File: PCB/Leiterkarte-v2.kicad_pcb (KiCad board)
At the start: 4 copper layers, 40.3 x 85.7 mm, 56 parts

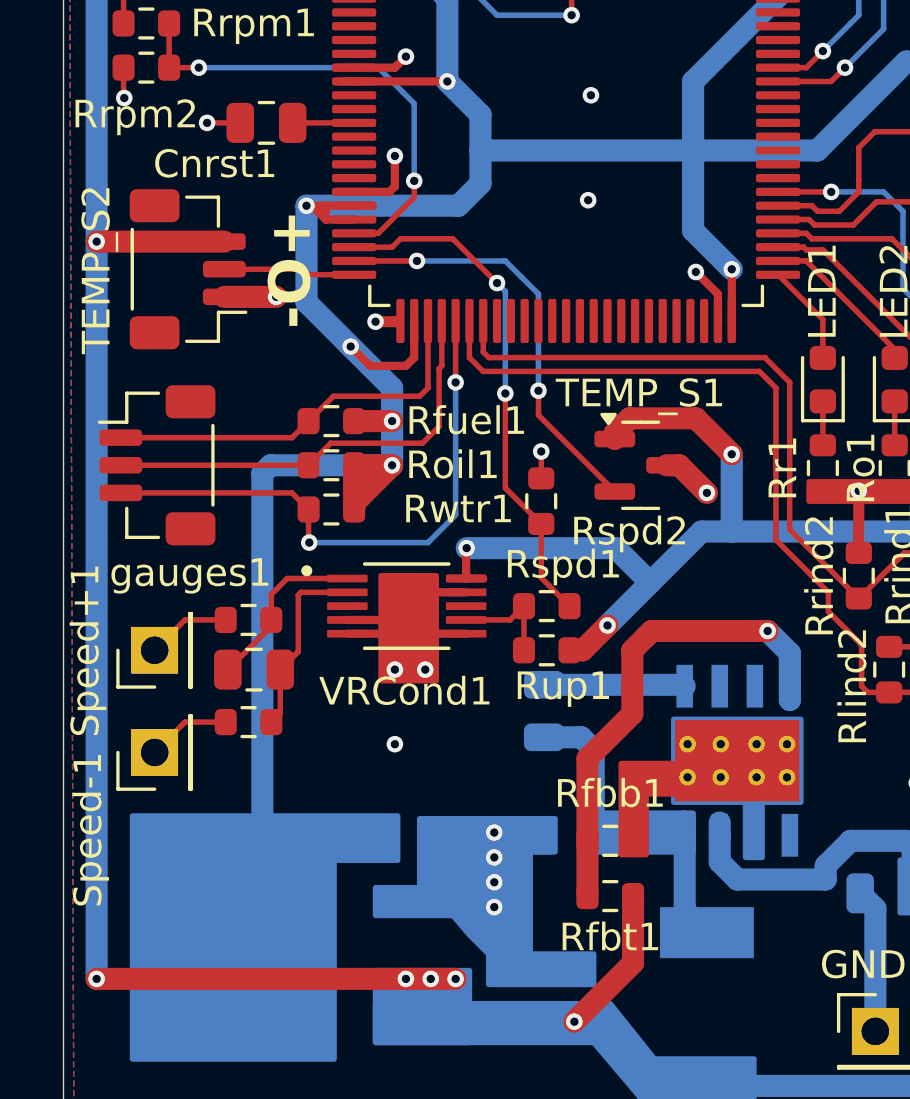
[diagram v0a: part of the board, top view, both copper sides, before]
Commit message: Replaced Speed- and Speed+ solder faces with JST SH connector
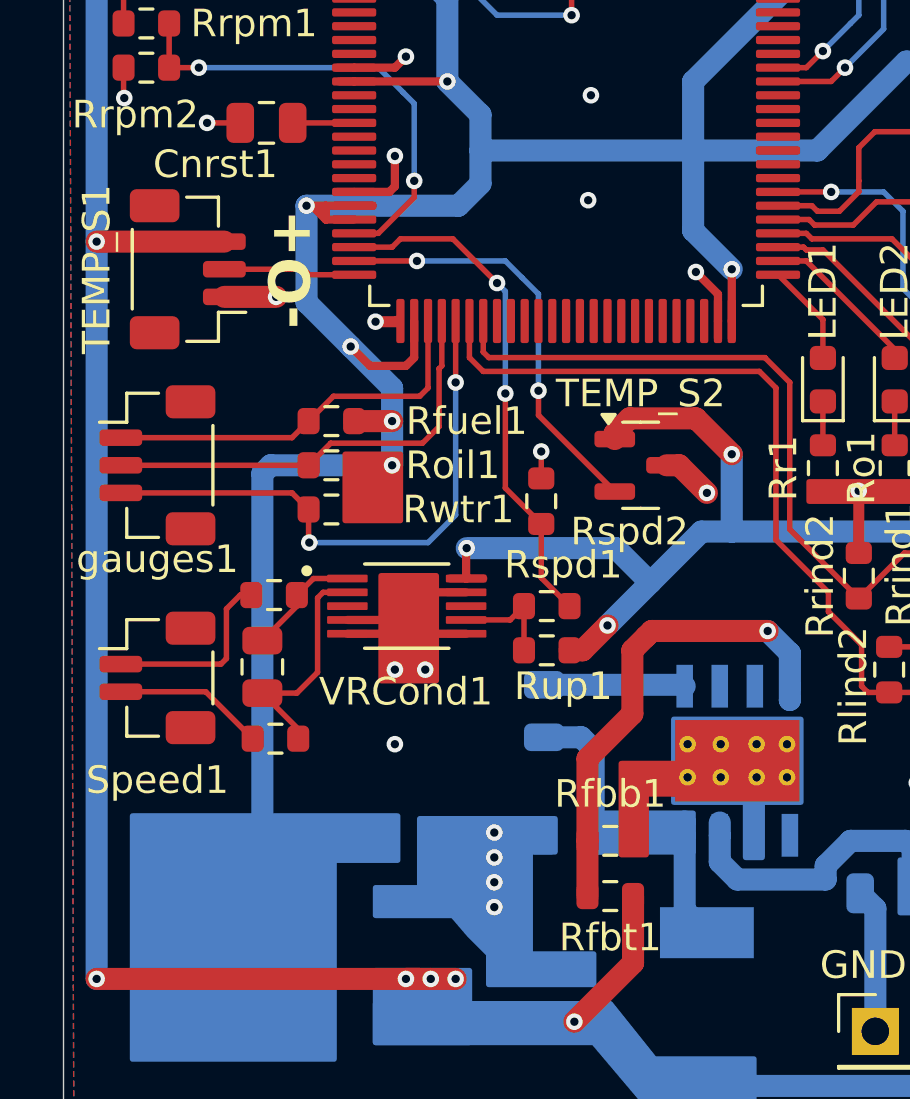
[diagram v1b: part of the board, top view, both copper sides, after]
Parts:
- removed Speed+1, Speed-1: Conn_01x01_Pin, Connector_PinHeader_2.54mm:PinHeader_1x01_P2.54mm_Vertical
- added Speed1: Conn_01x02_Pin, Connector_JST:JST_SH_BM02B-SRSS-TB_1x02-1MP_P1.00mm_Vertical, F.Cu at (147.8, 110.4)
- moved R2 1.29 mm to (152.0, 107.4)
- moved R1 1.14 mm to (152.1, 112.6)
- moved Cmax1 0.32 mm to (151.6, 110.0), turned to 90 degrees
- renumbered TEMP_S2 to TEMP_S1, TEMP_S1 to TEMP_S2
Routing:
- net +3.3V: track 155.6 -> 150.7 mm
- net Net-(Speed1-Pin_1): track 3.03 -> 6.81 mm
- net Net-(Speed1-Pin_2): track 3.03 -> 5.48 mm
- net Net-(VRCond1-IN+): track 6.37 -> 4.25 mm
- net Net-(VRCond1-IN-): track 6.83 -> 8.36 mm

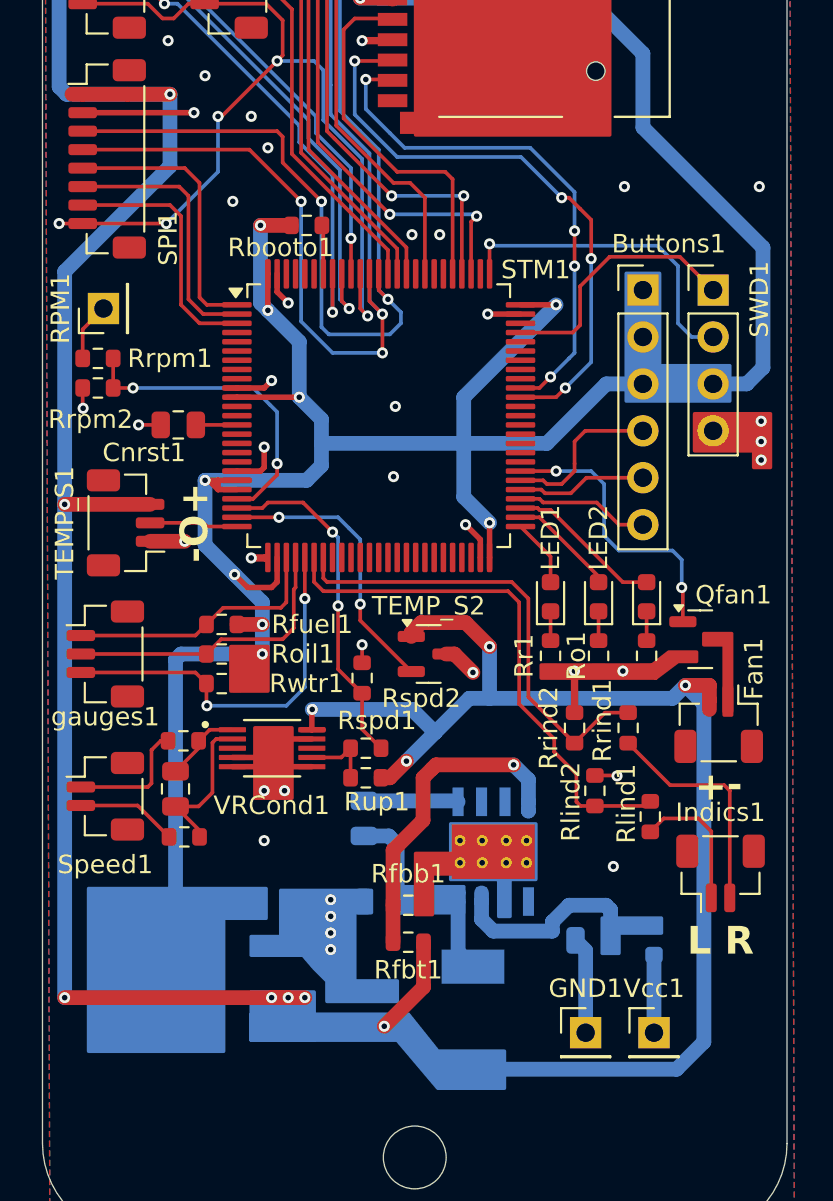
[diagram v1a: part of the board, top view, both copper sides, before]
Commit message: Replaced capacitor Cout2 and moved it to other side of the PCB;Updated some resistor footprints (to 0805);Some other stuff I forgot but similar :)
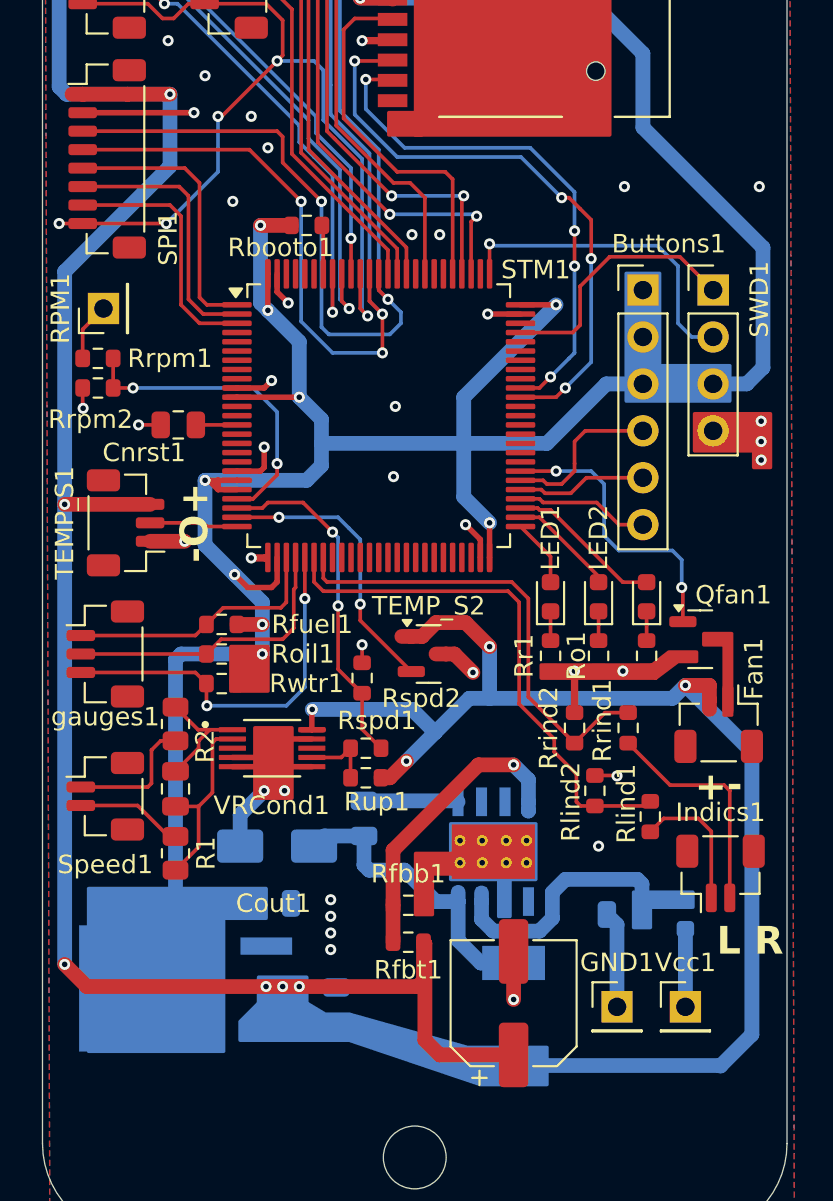
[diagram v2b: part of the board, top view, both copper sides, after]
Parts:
- Cout2: value 330uF -> 220uF; footprint Capacitor_SMD:C_0805_2012Metric -> Capacitor_SMD:CP_Elec_6.3x5.9; moved to F.Cu
- D1: footprint Diode_SMD:D_0805_2012Metric -> Diode_SMD:D_SMA
- R1, R2: footprint Resistor_SMD:R_0603_1608Metric -> Resistor_SMD:R_0805_2012Metric
- moved Cout2 7.01 mm to (169.9, 121.6)
- moved D1 6.35 mm to (157.1, 113.1)
- moved L1 2.21 mm to (169.9, 122.2)
- moved Cin1 2.20 mm to (175.9, 116.8)
- moved F1 2.20 mm to (179.2, 116.8)
- moved GND1 2.20 mm to (175.5, 121.8)
- moved Vcc1 2.20 mm to (179.2, 121.8)
- moved R2 1.01 mm to (151.6, 106.5), turned to 90 degrees
- moved R1 1.01 mm to (151.6, 113.5), turned to -90 degrees
- moved 3.3V1 0.55 mm to (150.1, 120.8)
- moved Cin2 0.28 mm to (160.3, 121.7)
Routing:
- net +5V: track 180.2 -> 193.6 mm, vias 12 -> 11
- net GND: track 67.4 -> 75.1 mm
- net Net-(5V1-PH): track 9.46 -> 16.5 mm
- net VCC: track 11.3 -> 14.1 mm
- net Net-(VRCond1-IN+): track 4.25 -> 6.60 mm
- net Net-(VRCond1-IN-): track 8.36 -> 10.1 mm
- net Net-(5V1-VSENSE): track 17.6 -> 16.3 mm

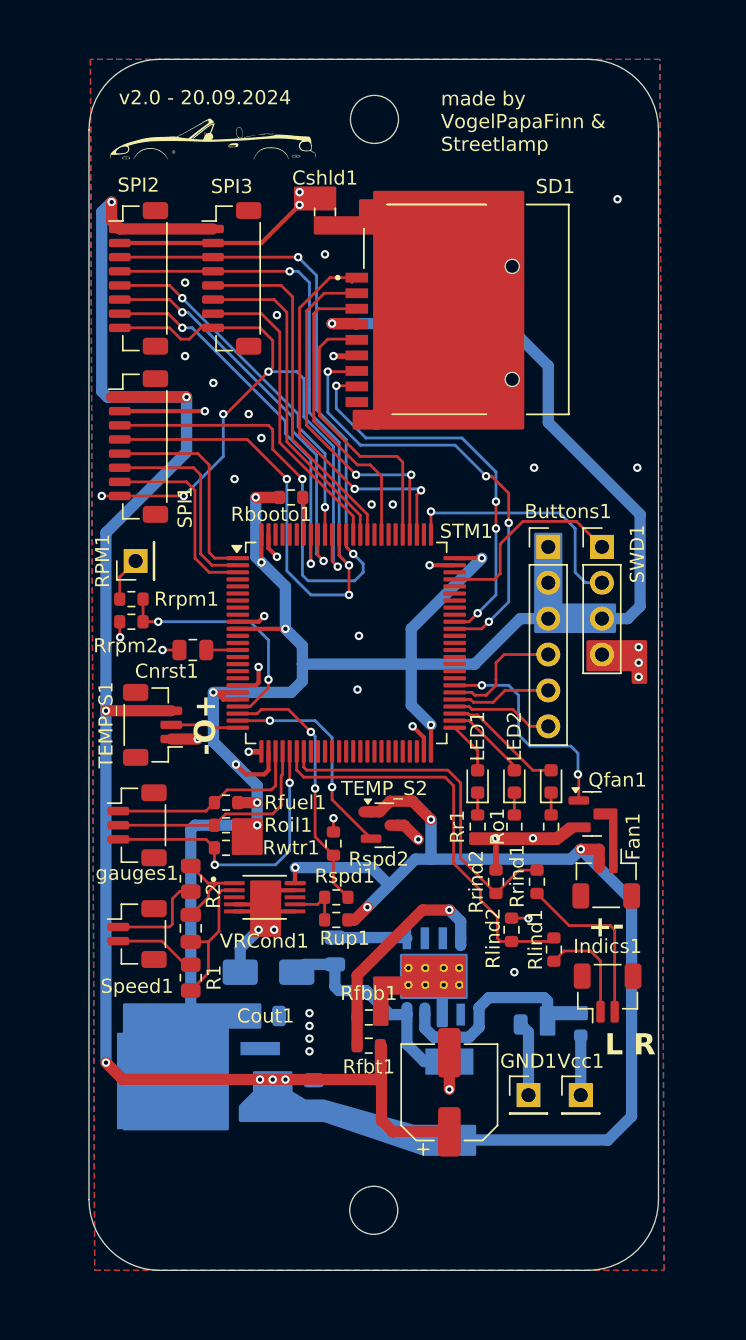
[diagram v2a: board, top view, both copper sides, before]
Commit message: Replaced STM32 with ESP32; Addec circuitry for ESP32; Removed LEDs; Added USB-C for flashing
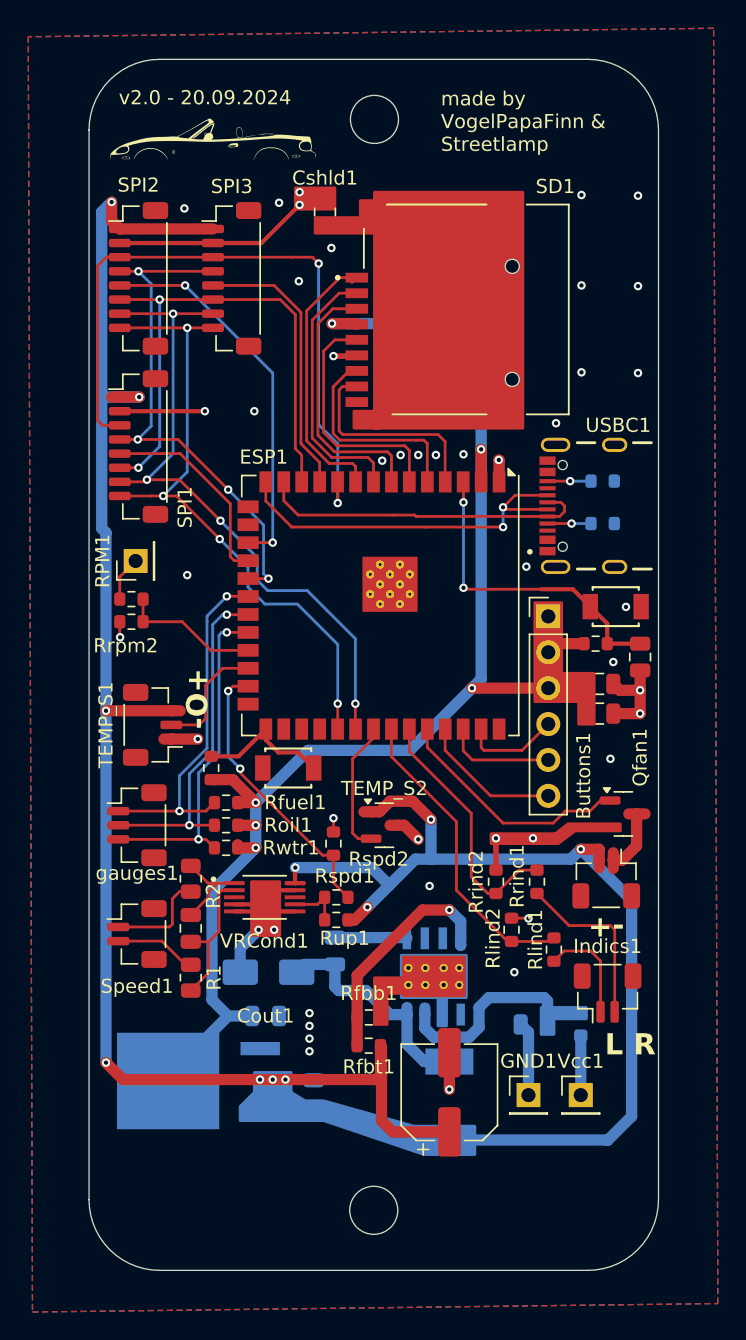
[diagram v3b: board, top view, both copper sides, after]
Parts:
- removed Cnrst1: 100nF, Capacitor_SMD:C_0805_2012Metric
- removed LED1: Red, LED_SMD:LED_0603_1608Metric
- removed LED2: Orange, LED_SMD:LED_0603_1608Metric
- removed LED3: Green, LED_SMD:LED_0603_1608Metric
- removed Rbooto1: 10K, Resistor_SMD:R_0603_1608Metric
- removed Rg1: 30, Resistor_SMD:R_0603_1608Metric
- removed Ro1, Rr1: 150, Resistor_SMD:R_0603_1608Metric
- removed STM1: STM32H743VITx, Package_QFP:LQFP-100_14x14mm_P0.5mm
- removed SWD1: Conn_01x04_Pin, Connector_PinHeader_2.54mm:PinHeader_1x04_P2.54mm_Vertical
- added Cen1: 1uF, Capacitor_SMD:C_0805_2012Metric, F.Cu at (183.4, 90.8)
- added Cesp1: 22uF, Capacitor_SMD:C_0805_2012Metric, F.Cu at (180.6, 94.8)
- added Cesp2: 0.1uF, Capacitor_SMD:C_0805_2012Metric, F.Cu at (180.6, 92.7)
- added ESP1: ESP32-S3-WROOM-1U, RF_Module:ESP32-S3-WROOM-1U, F.Cu at (165.0, 87.2)
- added ESP_BOOT1: SW_SPST, button:small_button, F.Cu at (158.5, 98.7)
- added ESP_RST1: SW_SPST, button:small_button, F.Cu at (181.7, 87.2)
- added Rboot1: 10k, Resistor_SMD:R_0603_1608Metric, F.Cu at (153.1, 98.7)
- added Resp1: 5.1k, Resistor_SMD:R_0603_1608Metric, F.Cu at (180.2, 89.8)
- added Rusb1: 5.1k, Resistor_SMD:R_0603_1608Metric, B.Cu at (180.8, 81.3)
- added Rusb2: 5.1k, Resistor_SMD:R_0603_1608Metric, B.Cu at (180.8, 78.3)
- added USBC1: USB4105-GF-A, USB-C 2.0:GCT_USB4105-GF-A, F.Cu at (181.6, 80.1)
- moved Buttons1 4.92 mm to (176.9, 87.9)
- moved Qfan1 2.21 mm to (182.2, 101.9)
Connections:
- SPI1 pad 6: DC1 -> DC
- SPI1 pad 7: RST1 -> RST
- SPI2 pad 6: DC2 -> DC
- SPI2 pad 7: RST2 -> RST
- SPI3 pad 6: DC3 -> DC
- SPI3 pad 7: RST3 -> RST
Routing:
- net +3.3V: track 150.7 -> 97.0 mm, vias 10 -> 6
- net RST: track 0.00 -> 47.9 mm, vias 0 -> 4
- net DC: track 0.00 -> 38.7 mm, vias 0 -> 2
- net DC2: track 28.8 -> 0.00 mm, vias 2 -> 0
- net RST2: track 27.8 -> 0.00 mm, vias 2 -> 0
- net USB_D+: track 0.00 -> 27.0 mm, vias 0 -> 2
- net CLK: track 64.1 -> 37.4 mm
- net USB_D-: track 0.00 -> 23.5 mm
- net DC3: track 23.5 -> 0.00 mm
- net Net-(ESP1-EN): track 0.00 -> 22.5 mm, vias 0 -> 2
- net RST3: track 21.7 -> 0.00 mm
- net SWCLK: track 17.6 -> 0.00 mm, vias 1 -> 0
- net DIN: track 65.2 -> 47.7 mm, vias 3 -> 2
- net SD_DAT0: track 32.4 -> 15.1 mm, vias 4 -> 0
- net DC1: track 14.5 -> 0.00 mm
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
